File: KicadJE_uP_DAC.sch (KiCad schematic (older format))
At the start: 57 parts, among them J101 ADSR1, J102 ADSR2, J103 ADSR1, J104 ADSR2, J105 ADSR1-G8, J106 ADSR2-G8, J107 ADSR4-G8, J108 ADSR3-G8, P101 Doepfer_Power_16pin

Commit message: MCP4822
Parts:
- added U?: MCP4822, symbol Analog_DAC:MCP4822
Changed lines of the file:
@@
+	1    0    0    -1
+$EndComp
+$Comp
+L Analog_DAC:MCP4822 U?
+U 1 1 5CE0D72D
+P 8900 4025
+F 0 "U?" H 8900 4606 50  0000 C CNN
+F 1 "MCP4822" H 8900 4515 50  0000 C CNN
+F 2 "" H 9700 3725 50  0001 C CNN
+F 3 "http://ww1.microchip.com/downloads/en/DeviceDoc/20002249B.pdf" H 9700 3725 50  0001 C CNN
+	1    8900 4025
 	1    0    0    -1
 $EndComp

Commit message: Hierarchical ATMega32 pins
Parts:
- added C? (x2): 100n, Capacitor_SMD:C_0805_2012Metric_Pad1.15x1.40mm_HandSolder, symbol Device:C
- added C? (x2): 100n, Capacitor_SMD:C_1206_3216Metric_Pad1.42x1.75mm_HandSolder, symbol Device:C
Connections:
- net +12V: now also C?.2, C?.2
- net -12V: now also C?.2, C?.2
- net GND: now also C?.1, C?.1, C?.1, C?.1
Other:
- moved on the sheet: C101, C102, C103, C104, D101, D102, D103, D104, D105, D106, D107, D108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

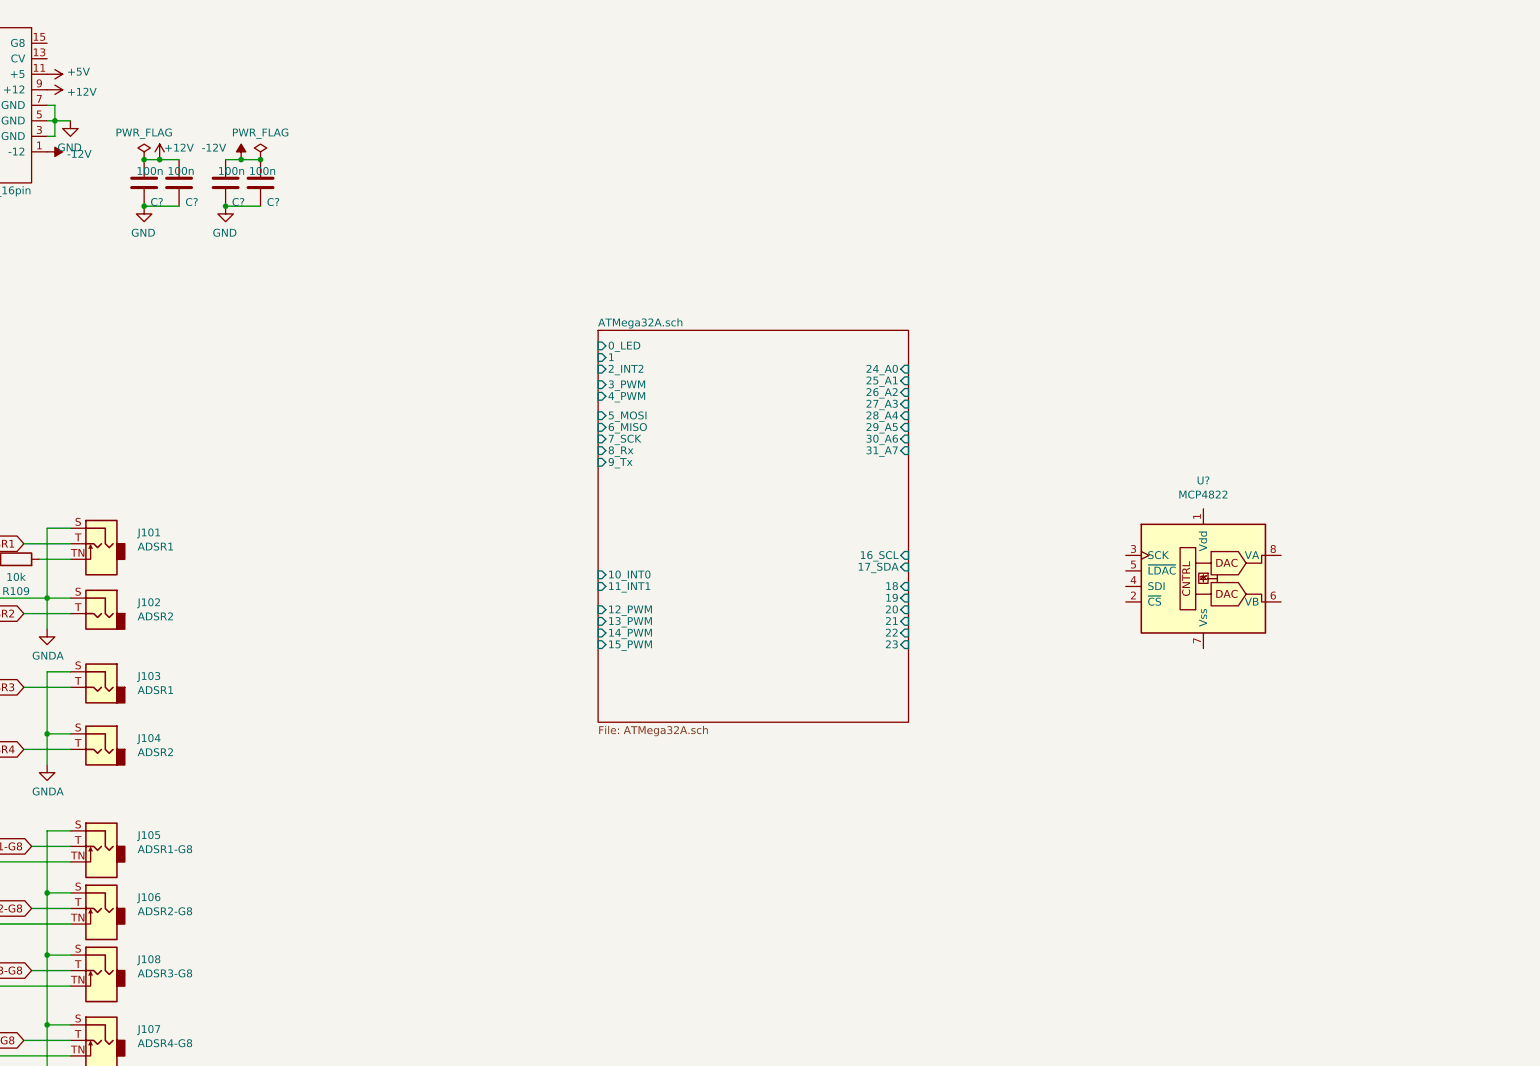
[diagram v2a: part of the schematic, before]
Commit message: 2x Sallen Key LP out from DAC
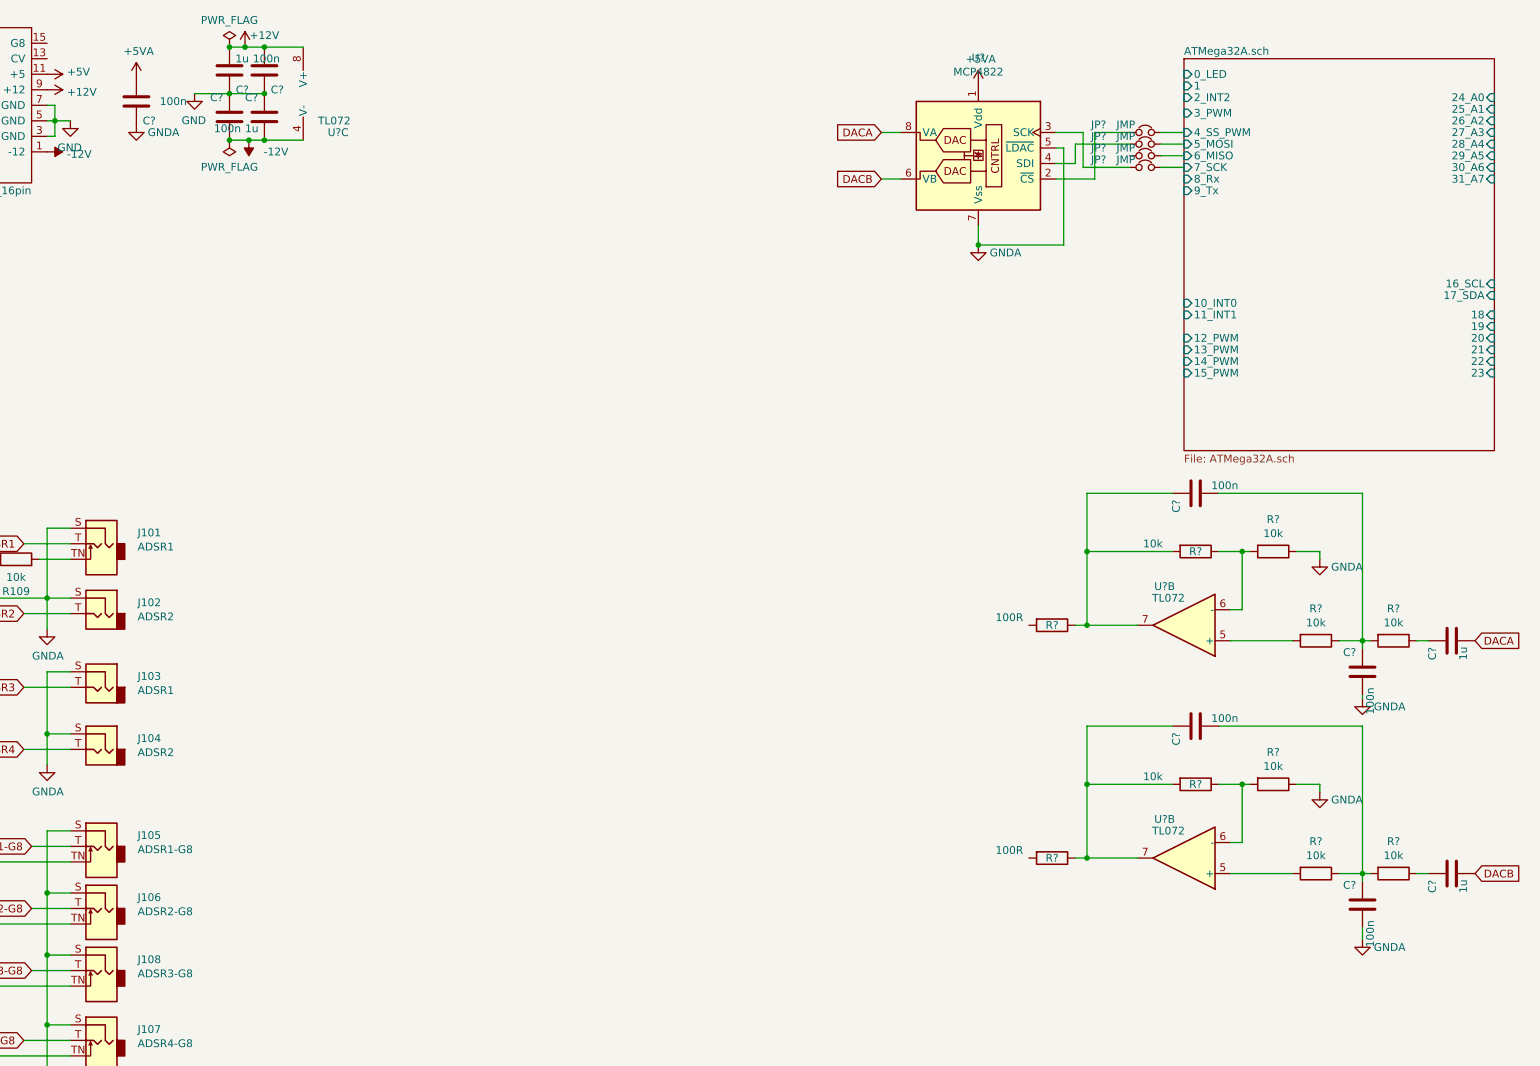
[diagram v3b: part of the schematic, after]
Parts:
- added C? (x5): 100n, Capacitor_SMD:C_0805_2012Metric_Pad1.15x1.40mm_HandSolder, symbol Device:C
- added C? (x2): 1u, Capacitor_SMD:C_1206_3216Metric_Pad1.42x1.75mm_HandSolder, symbol Device:C
- added JP? (x4): JMP, Connector_PinSocket_2.54mm:PinSocket_1x02_P2.54mm_Vertical, symbol Device:Jumper_NC_Small
- added R? (x8): 10k, Resistor_SMD:R_0805_2012Metric_Pad1.15x1.40mm_HandSolder, symbol Device:R
- added R? (x2): 100R, Resistor_SMD:R_0805_2012Metric_Pad1.15x1.40mm_HandSolder, symbol Device:R
- added U? (x3): TL072, symbol Amplifier_Operational:TL072
- C? (x2): value 100n -> 1u
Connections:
- net +12V: now also U?.8 (V+)
- net -12V: now also U?.4 (V-)
- net ATMega32A.sch/5_MOSI: now also JP?.2
- net ATMega32A.sch/6_MISO: now also JP?.2
- net ATMega32A.sch/7_SCK: now also JP?.2
- net GNDA: now also U?.5 (~LDAC), U?.7 (Vss), C?.1, C?.2, C?.2, R?.1, R?.1
- net +5VA: now reaches U?.1 (Vdd)
- net +5VA: now also C?.2
- net at U?.2 (~CS): now also JP?.1
- net at U?.3 (SCK): now also JP?.1
- net at U?.4 (SDI): now also JP?.1
- net DACB: now reaches U?.6 (VB)
- net DACB: now also C?.2
- net DACA: now reaches U?.8 (VA)
- net DACA: now also C?.2
- new net: R?.2, U?.5 (+) (x2)
- new net: R?.1, R?.2, U?.6 (-) (x2)
- new net: C?.1, R?.1, R?.2, U?.7 (x2)
- new net: C?.1, R?.1 (x2)
- new net: C?.1, C?.2, R?.1, R?.2 (x2)
- new net ATMega32A.sch/4_SS_PWM: JP?.2
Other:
- moved on the sheet: C?, U?

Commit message: CV and Input protection
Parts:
- removed C?: 1u, Capacitor_SMD:C_1206_3216Metric_Pad1.42x1.75mm_HandSolder, symbol Device:C
- removed C? (x2): 100n, Capacitor_SMD:C_0805_2012Metric_Pad1.15x1.40mm_HandSolder, symbol Device:C
- removed J102: ADSR2, AJ-Dropbox-Kicad:PJ301SM, symbol Connector:AudioJack2
- removed J106: ADSR2-G8, AJ-Dropbox-Kicad:PJ301SM, symbol Connector:AudioJack2_SwitchT
- removed R109, R110, R? (x4): 10k, Resistor_SMD:R_0805_2012Metric_Pad1.15x1.40mm_HandSolder, symbol Device:R
- removed R?: 100R, Resistor_SMD:R_0805_2012Metric_Pad1.15x1.40mm_HandSolder, symbol Device:R
- removed U?: TL072, symbol Amplifier_Operational:TL072
- added C?: 1u, Capacitor_SMD:C_1206_3216Metric_Pad1.42x1.75mm_HandSolder, symbol Device:C
- added C? (x2): 100n, Capacitor_SMD:C_0805_2012Metric_Pad1.15x1.40mm_HandSolder, symbol Device:C
- added D? (x6): 1N1007, Diode_SMD:D_SOD-123, symbol Device:D
- added R? (x7): 10k, Resistor_SMD:R_0805_2012Metric_Pad1.15x1.40mm_HandSolder, symbol Device:R
- added R?: 100R, Resistor_SMD:R_0805_2012Metric_Pad1.15x1.40mm_HandSolder, symbol Device:R
- added RV? (x2): 100k, Potentiometer_THT:Potentiometer_China_RK09_Single_Vertical_AJ, symbol Device:R_POT
- added U?: TL072, symbol Amplifier_Operational:TL072
- J101: value ADSR1 -> CV1
- J103: value ADSR1 -> OUT1
- J104: value ADSR2 -> OUT2
- J105: value ADSR1-G8 -> CV2
- J107: value ADSR4-G8 -> IN2
- J108: value ADSR3-G8 -> IN1
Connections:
- net 28_A4 is gone; now on an unnamed net: RV105.2
- net +5V: now also D?.1 (K), D?.1 (K), D?.1 (K); no longer D119.1 (K), RV104.3, RV105.3
- net ADSR1: no longer J101.T
- net ADSR3: no longer J103.T
- net ADSR3-G8: no longer J108.T
- net ADSR4: no longer J104.T
- net ADSR4-G8: no longer J107.T
- net DACA: now also C?.2
- net GND: now also RV104.3, RV105.3, RV?.3, RV?.3; no longer RV104.1, RV105.1
- net GNDA: now also C?.2, D?.2 (A), D?.2 (A), D?.2 (A), R?.1
- net at J101.TN: now also J105.T, RV104.1
- net OUT2: now reaches R?.2
- net OUT2: now also J104.T
- net 10_INT0: no longer names the net of R105.1
- net 24_A0 renamed Duty
- net 27_A3: no longer names the net of RV104.2
- net 27_A3: now also R?.1
- net 29_A5 renamed Wave
- net ADSR1-G8 renamed CV1
- net CV1: no longer J105.T
- new net: J101.T, J105.TN, RV105.1
- new net: J107.TN, J108.T, RV?.1
- new net: J107.T, J108.TN, RV?.1
- new net: R?.2, U?.5 (+)
- new net: R?.1, R?.2, U?.6 (-)
- new net: C?.1, R?.1, R?.2, U?.7
- new net: C?.1, R?.1
- new net: C?.1, C?.2, R?.1, R?.2
- new net: R?.1, RV?.2 (x2)
- new net CV2: D?.1 (K), D?.2 (A), R?.2
- new net IN1: D?.1 (K), D?.2 (A), R?.2
- new net IN2: D?.1 (K), D?.2 (A), R?.2
- new net OUT1: J103.T, R?.2
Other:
- moved on the sheet: C?, D117, D118, J101, J103, J104, J105, J107, J108, JP?, R105, R?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

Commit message: LED Matrix 3x4
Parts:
- removed C102, C104: 1u, Capacitor_SMD:C_0805_2012Metric_Pad1.15x1.40mm_HandSolder, symbol Device:C
- removed C103: 100n, Capacitor_SMD:C_0805_2012Metric_Pad1.15x1.40mm_HandSolder, symbol Device:C
- removed D104, D108, D112, D116: LED, LED_THT:LED_D3.0mm, symbol Device:LED
- removed D119, D120, D121, D122, D123, D124: 1N1007, Diode_SMD:D_SOD-123, symbol Device:D
- removed R101: 100R, Resistor_SMD:R_0805_2012Metric_Pad1.15x1.40mm_HandSolder, symbol Device:R
- removed R102, R104: 100r, Resistor_SMD:R_0805_2012Metric_Pad1.15x1.40mm_HandSolder, symbol Device:R
- removed R106, R107, R108, R112, R114: 10k, Resistor_SMD:R_0805_2012Metric_Pad1.15x1.40mm_HandSolder, symbol Device:R
- removed R113: 1k, Resistor_SMD:R_0805_2012Metric_Pad1.15x1.40mm_HandSolder, symbol Device:R
- removed RV102, RV103, RV? (x2): 100k, Potentiometer_THT:Potentiometer_China_RK09_Single_Vertical_AJ, symbol Device:R_POT
- added R?: 100R, Resistor_SMD:R_0805_2012Metric_Pad1.15x1.40mm_HandSolder, symbol Device:R
- added R? (x5): 100R, Resistor_SMD:R_0805_2012Metric_Pad1.15x1.40mm_HandSolder, symbol Device:R_Small
- added SW?: SW_SPDT, symbol Switch:SW_SPDT
- R103: symbol Device:R -> Device:R_Small
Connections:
- net 1 is gone; now on net ATMega32A.sch/18: R103.1
- net 12_PWM is gone; now on net ATMega32A.sch/12_PWM: R111.1
- net 18: now also R103.2
- net 19: now also R?.2
- net 20: now also R?.2
- net 21: now also R?.2
- net 22: now also D101.1 (K), D105.1 (K), D109.1 (K), D113.1 (K), R?.2
- net 23: now also D102.1 (K), D106.1 (K), D110.1 (K), D114.1 (K), R?.2
- net ATMega32A.sch/0_LED: now also R?.1
- net ATMega32A.sch/1: now also SW?.3 (C)
- net ATMega32A.sch/19: now also R?.1
- net ATMega32A.sch/20: now also R?.1
- net ATMega32A.sch/21: now also R?.1
- net ATMega32A.sch/22: now also R?.1
- net ATMega32A.sch/23: now also R?.1
- net ATMega32A.sch/2_INT2: now also SW?.1 (A)
- net GND: now also C101.1, SW?.2 (B)
- net GNDA: no longer C101.1
- net at J107.TN, J108.T: now also R?.1
- net at J107.T, J108.TN: now also R?.1
- net 0: now reaches D103.1 (K), D107.1 (K), D111.1 (K), D115.1 (K)
- net 0: now also R?.2; no longer R103.2
- net ADSR1 renamed PWM12
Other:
- moved on the sheet: C101, D101, D102, D103, D105, D106, D107, D109, D110, D111, D113, D114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

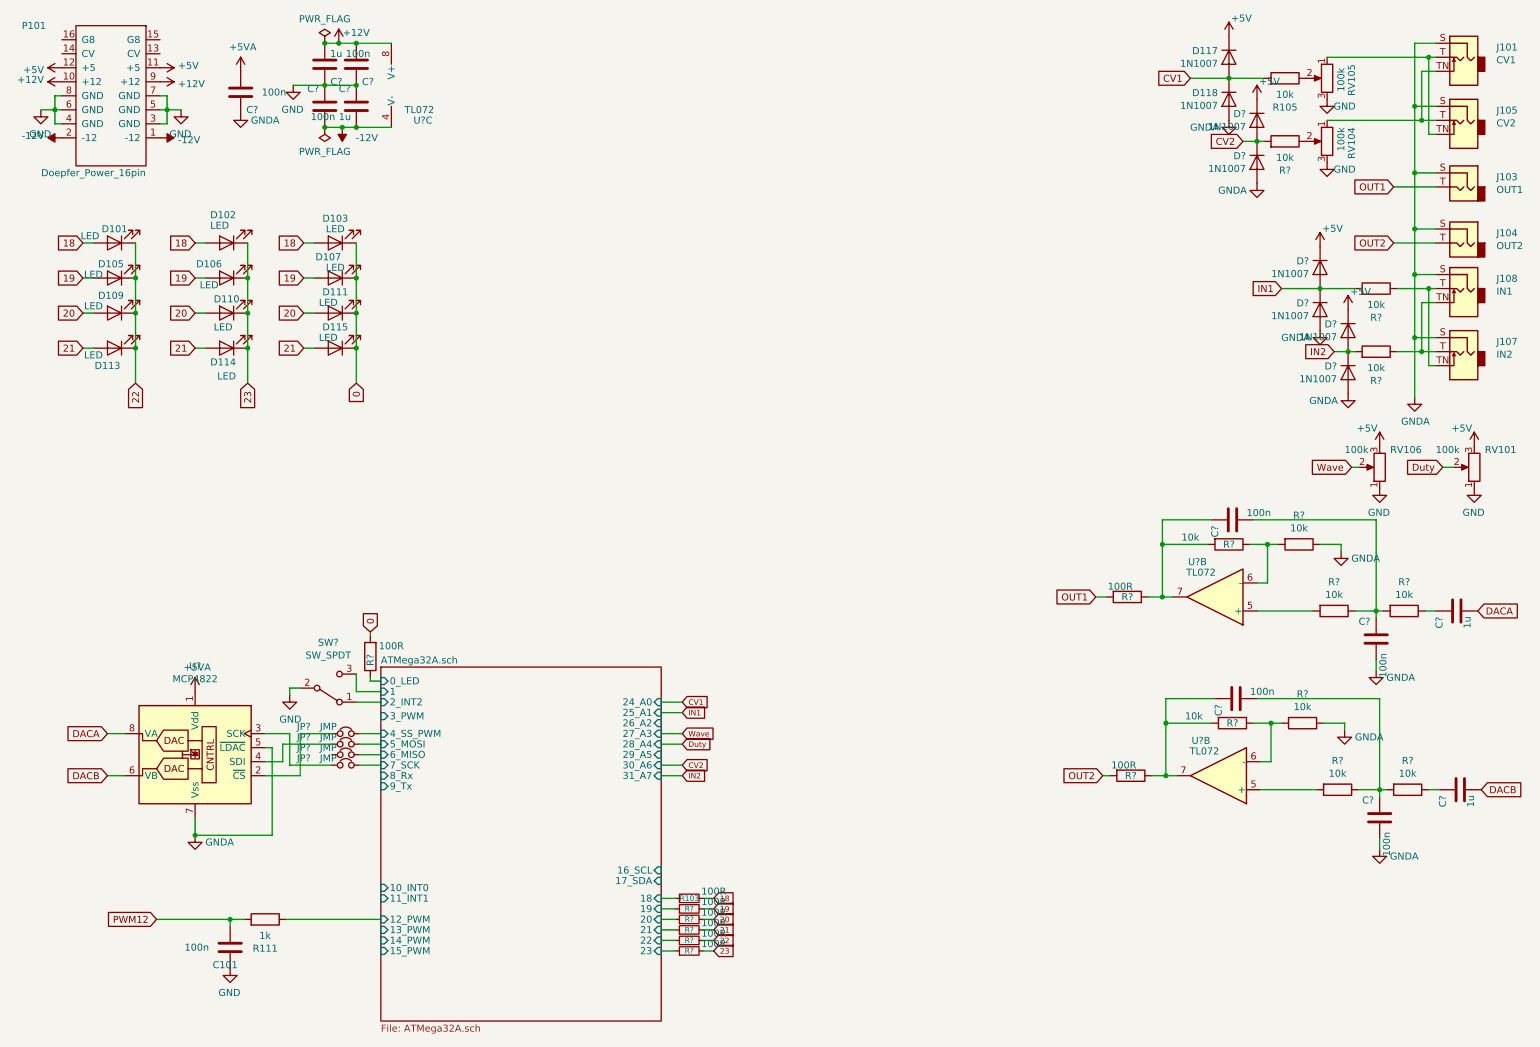
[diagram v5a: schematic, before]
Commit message: Dual uP hierarchy
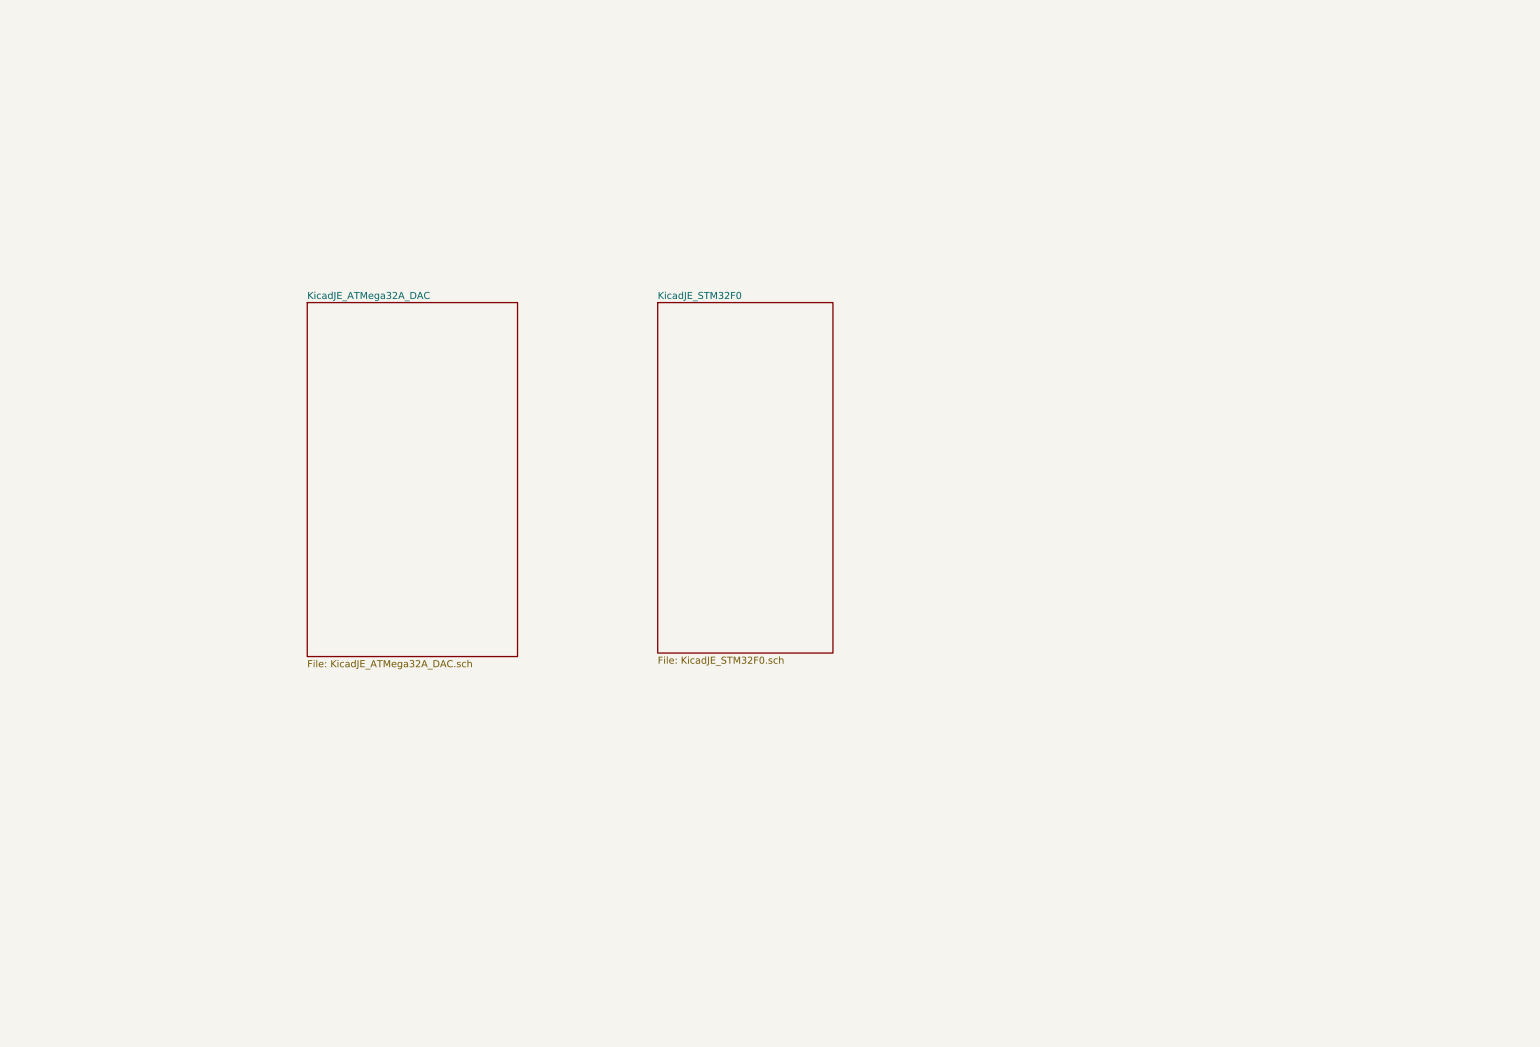
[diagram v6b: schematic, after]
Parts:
- removed C101, C? (x7): 100n, Capacitor_SMD:C_0805_2012Metric_Pad1.15x1.40mm_HandSolder, symbol Device:C
- removed C? (x4): 1u, Capacitor_SMD:C_1206_3216Metric_Pad1.42x1.75mm_HandSolder, symbol Device:C
- removed D101, D102, D103, D105, D106, D107, D109, D110, D111, D113, D114, D115: LED, LED_THT:LED_D3.0mm, symbol Device:LED
- removed D117, D118, D? (x6): 1N1007, Diode_SMD:D_SOD-123, symbol Device:D
- removed J101: CV1, AJ-Dropbox-Kicad:PJ301SM, symbol Connector:AudioJack2_SwitchT
- removed J103: OUT1, AJ-Dropbox-Kicad:PJ301SM, symbol Connector:AudioJack2
- removed J104: OUT2, AJ-Dropbox-Kicad:PJ301SM, symbol Connector:AudioJack2
- removed J105: CV2, AJ-Dropbox-Kicad:PJ301SM, symbol Connector:AudioJack2_SwitchT
- removed J107: IN2, AJ-Dropbox-Kicad:PJ301SM, symbol Connector:AudioJack2_SwitchT
- removed J108: IN1, AJ-Dropbox-Kicad:PJ301SM, symbol Connector:AudioJack2_SwitchT
- removed JP? (x4): JMP, Connector_PinSocket_2.54mm:PinSocket_1x02_P2.54mm_Vertical, symbol Device:Jumper_NC_Small
- removed P101: Doepfer_Power_16pin, Connectors_IDC:IDC-Header_2x08_Pitch2.54mm_Straight, symbol Eurorack:Doepfer_Power_16pin
- removed R103, R? (x5): 100R, Resistor_SMD:R_0805_2012Metric_Pad1.15x1.40mm_HandSolder, symbol Device:R_Small
- removed R105, R? (x11): 10k, Resistor_SMD:R_0805_2012Metric_Pad1.15x1.40mm_HandSolder, symbol Device:R
- removed R111: 1k, Resistor_SMD:R_0805_2012Metric_Pad1.15x1.40mm_HandSolder, symbol Device:R
- removed R? (x3): 100R, Resistor_SMD:R_0805_2012Metric_Pad1.15x1.40mm_HandSolder, symbol Device:R
- removed RV101, RV104, RV105, RV106: 100k, Potentiometer_THT:Potentiometer_China_RK09_Single_Vertical_AJ, symbol Device:R_POT
- removed SW?: SW_SPDT, symbol Switch:SW_SPDT
- removed U?: MCP4822, symbol Analog_DAC:MCP4822
- removed U? (x3): TL072, symbol Amplifier_Operational:TL072
